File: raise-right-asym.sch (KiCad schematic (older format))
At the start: 123 parts, among them IC1 ATTINY88-A, J1 USB_C_Receptacle_16pin, P1 CONN_01X01, P2 CONN_01X01, P3 CONN_01X01, P4 CONN_01X01, P8 CONN_02X03, Q1 PMOS, -3.6A, 0.02R, SW1 kailh hot plug sockets, SW10 kailh hot plug sockets, SW11 kailh hot plug sockets, SW12 kailh hot plug sockets, SW13 kailh hot plug sockets, SW14 kailh hot plug sockets, SW15 kailh hot plug sockets, SW17 kailh hot plug sockets, SW18 kailh hot plug sockets, SW19 kailh hot plug sockets, SW2 kailh hot plug sockets, SW20 kailh hot plug sockets, SW21 kailh hot plug sockets, SW22 kailh hot plug sockets, SW23 kailh hot plug sockets, SW24 kailh hot plug sockets, SW25 kailh hot plug sockets, SW26 kailh hot plug sockets, SW27 kailh hot plug sockets, SW28 kailh hot plug sockets, SW29 kailh hot plug sockets, SW3 kailh hot plug sockets, SW30 kailh hot plug sockets, SW31 kailh hot plug sockets, SW32 kailh hot plug sockets, SW33 kailh hot plug sockets, SW34 kailh hot plug sockets, SW4 kailh hot plug sockets, SW5 kailh hot plug sockets, SW6 kailh hot plug sockets, SW7 kailh hot plug sockets, SW9 kailh hot plug sockets, T1 CONN_01X01, T2 CONN_01X01, T3 CONN_01X01, U1 ss39et

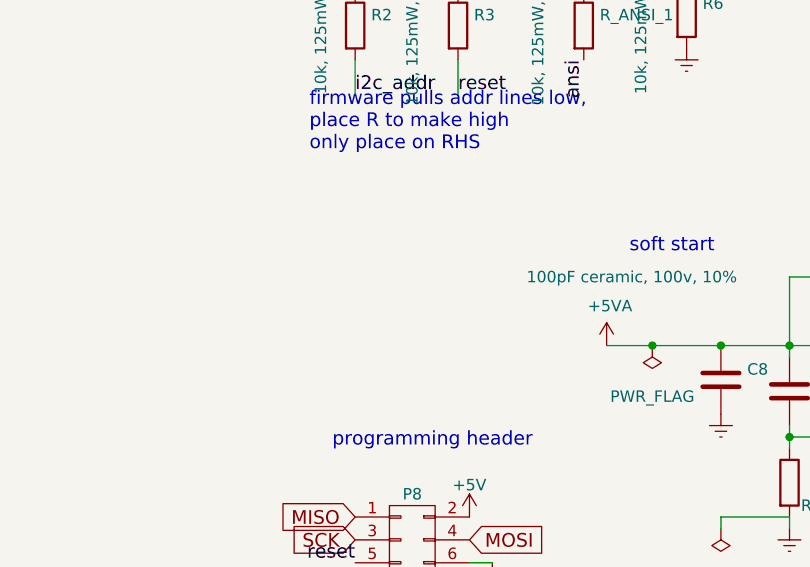
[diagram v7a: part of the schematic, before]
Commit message: added esd protection to sda/scl/reset/cc
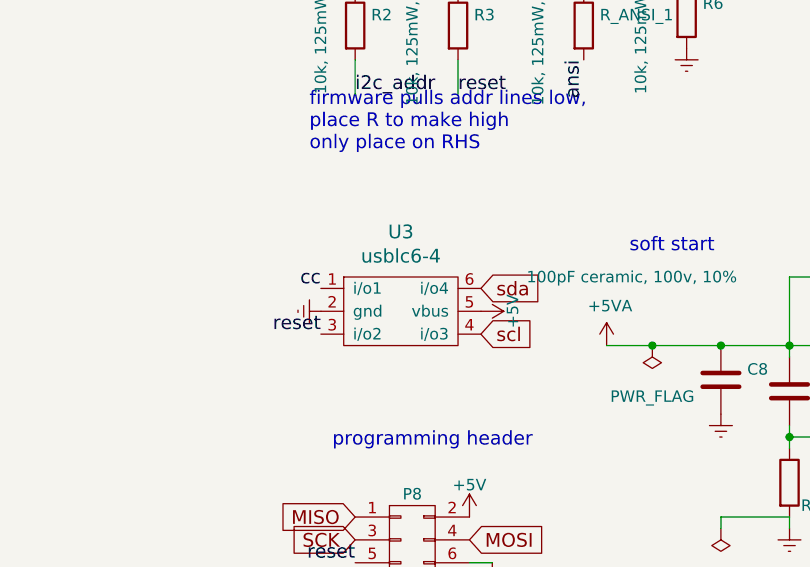
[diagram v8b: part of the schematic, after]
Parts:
- added U3: usblc6-4, raise_fp:SOT-23-6, symbol usblc6-4
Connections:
- net +5V: now also U3.5 (vbus)
- net Earth: now also U3.2 (gnd)
- net cc: now also U3.1 (i/o1)
- net reset: now also U3.3 (i/o2)
- net scl: now also U3.4 (i/o3)
- net sda: now also U3.6 (i/o4)
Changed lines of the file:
@@
 LIBS:test-jig
 LIBS:usb_c_16pin
+LIBS:usblc6-4
 EELAYER 26 0
 EELAYER END
@@
 F1 "ledmatrix.sch" 60
 $EndSheet
+$Comp
+L usblc6-4 U3
+U 1 1 5C632C8B
+P 1100 6450
+F 0 "U3" H 1100 6797 60  0000 C CNN
+F 1 "usblc6-4" H 1100 6691 60  0000 C CNN
+F 2 "raise_fp:SOT-23-6" H 1100 6450 60  0001 C CNN
+F 3 "" H 1100 6450 60  0001 C CNN
+	1    1100 6450
+	1    0    0    -1
+$EndComp
+Text GLabel 1450 6350 2    60   Input ~ 0
+sda
+Text GLabel 1450 6550 2    60   Input ~ 0
+scl
+Text Label 750  6350 2    60   ~ 0
+cc
+Text Label 750  6550 2    60   ~ 0
+reset
+$Comp
+L +5V #PWR040
+U 1 1 5C63398B
+P 1450 6450
+F 0 "#PWR040" H 1450 6300 50  0001 C CNN
+F 1 "+5V" H 1450 6590 50  0000 C CNN
+F 2 "" H 1450 6450 60  0000 C CNN
+F 3 "" H 1450 6450 60  0000 C CNN
+	1    1450 6450
+	0    1    1    0
+$EndComp
+$Comp
+L Earth #PWR041
+U 1 1 5C633B0A
+P 750 6450
+F 0 "#PWR041" H 750 6200 50  0001 C CNN
+F 1 "Earth" H 750 6300 50  0001 C CNN
+F 2 "" H 750 6450 60  0000 C CNN
+F 3 "" H 750 6450 60  0000 C CNN
+	1    750  6450
+	0    1    1    0
+$EndComp
 $EndSCHEMATC
